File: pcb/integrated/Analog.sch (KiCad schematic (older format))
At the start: 47 parts, among them J5001 Conn_Coaxial, U5001 74LVC1G3157GW, U5002 TLV3501AIDBVR, U5003 74LVC1G3157GW, U5004 MCP6561-OT

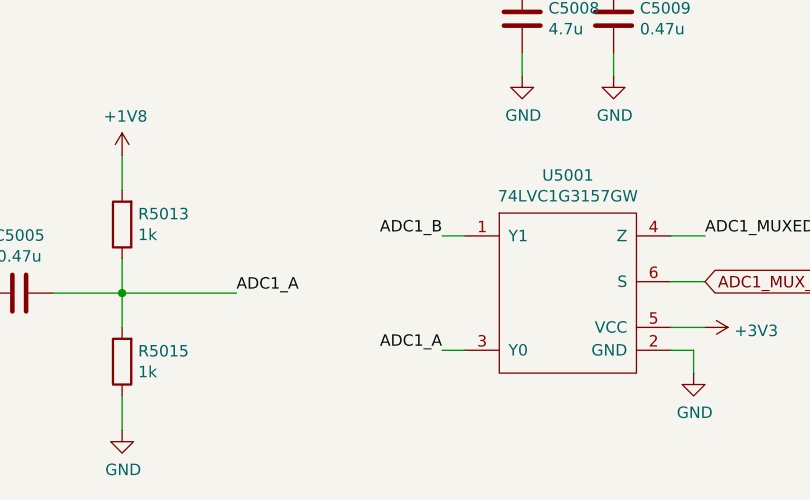
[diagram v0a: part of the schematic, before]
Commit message: schematic fixes and component placement
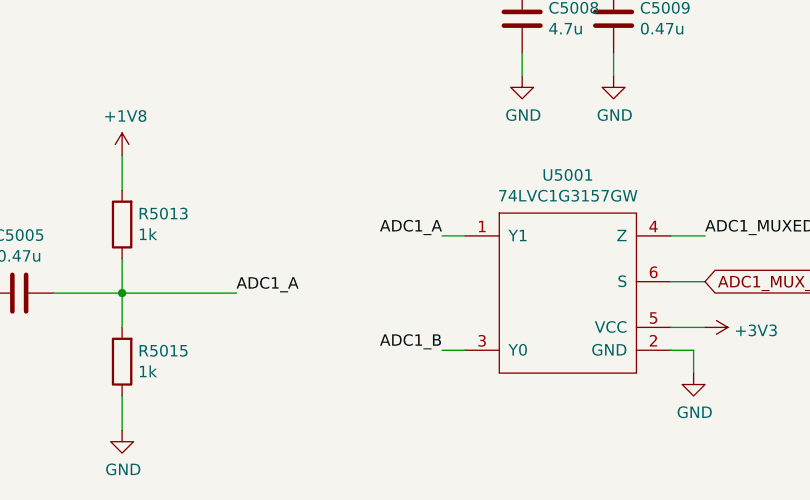
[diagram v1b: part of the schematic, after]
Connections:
- net ADC1_A: now also U5001.1 (Y1); no longer U5001.3 (Y0)
- net ADC1_B: now also U5001.3 (Y0); no longer U5001.1 (Y1)
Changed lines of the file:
@@
 Wire Wire Line
 	5150 7150 5050 7150
-Text Label 5050 7150 2    50   ~ 0
+Text Label 5050 6650 2    50   ~ 0
 ADC1_A
 $Comp
@@
 Text Label 2100 2350 0    50   ~ 0
 ADC1_B
-Text Label 5050 6650 2    50   ~ 0
+Text Label 5050 7150 2    50   ~ 0
 ADC1_B
 Wire Wire Line

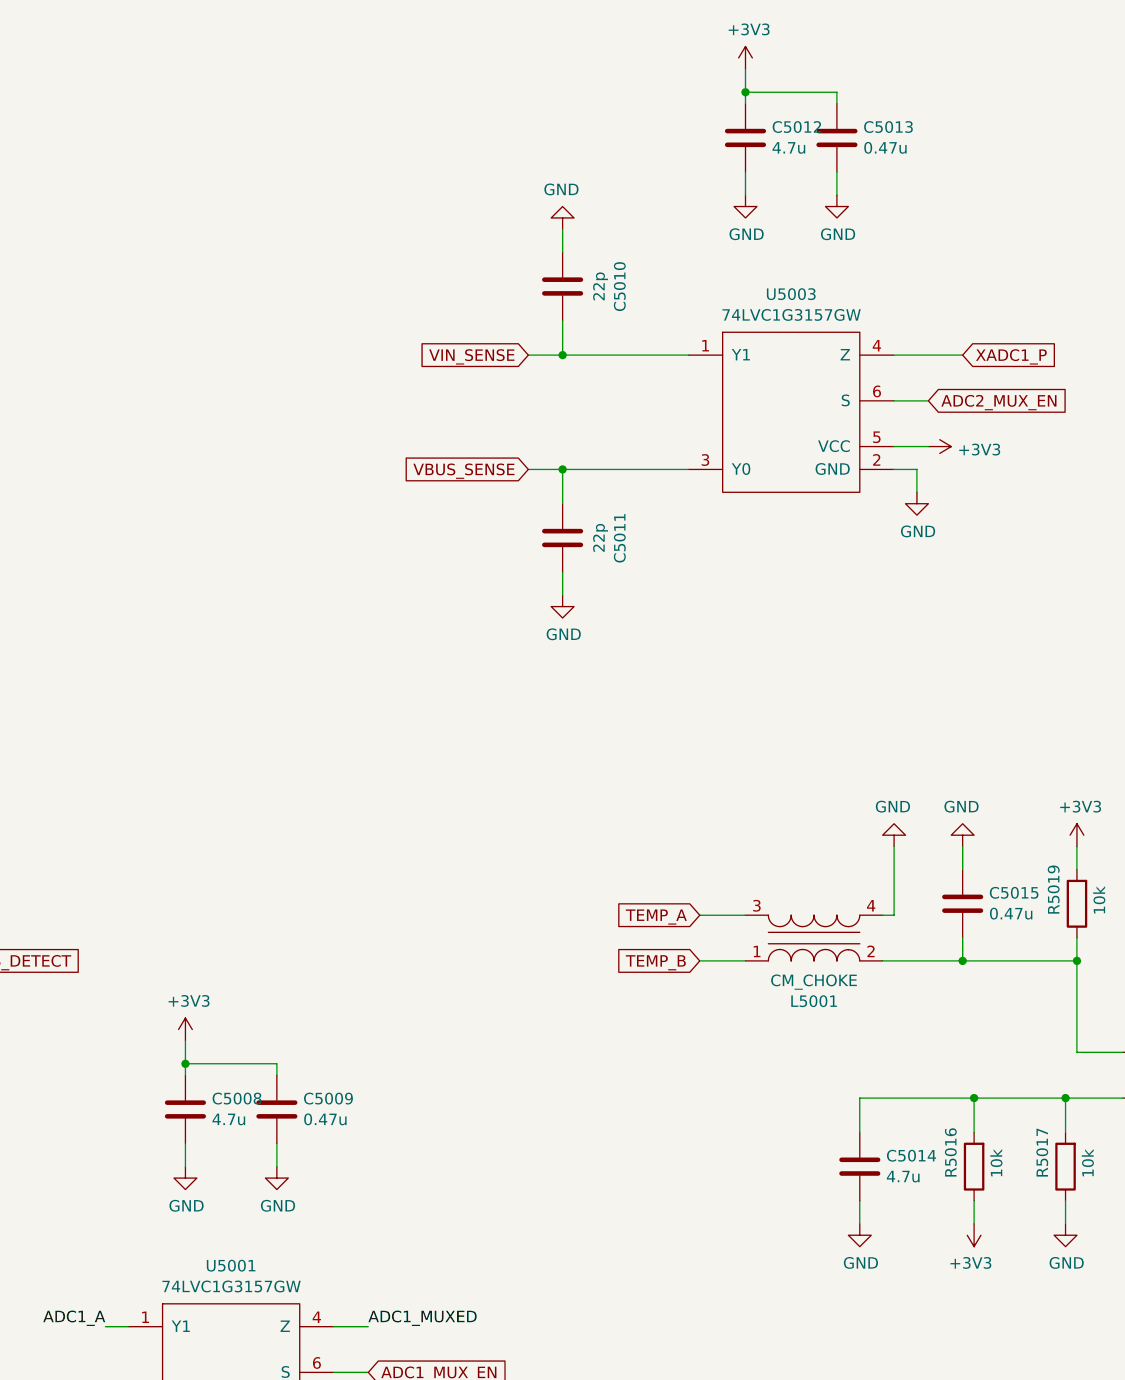
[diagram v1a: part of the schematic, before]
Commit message: routing, all componens placed on PCB
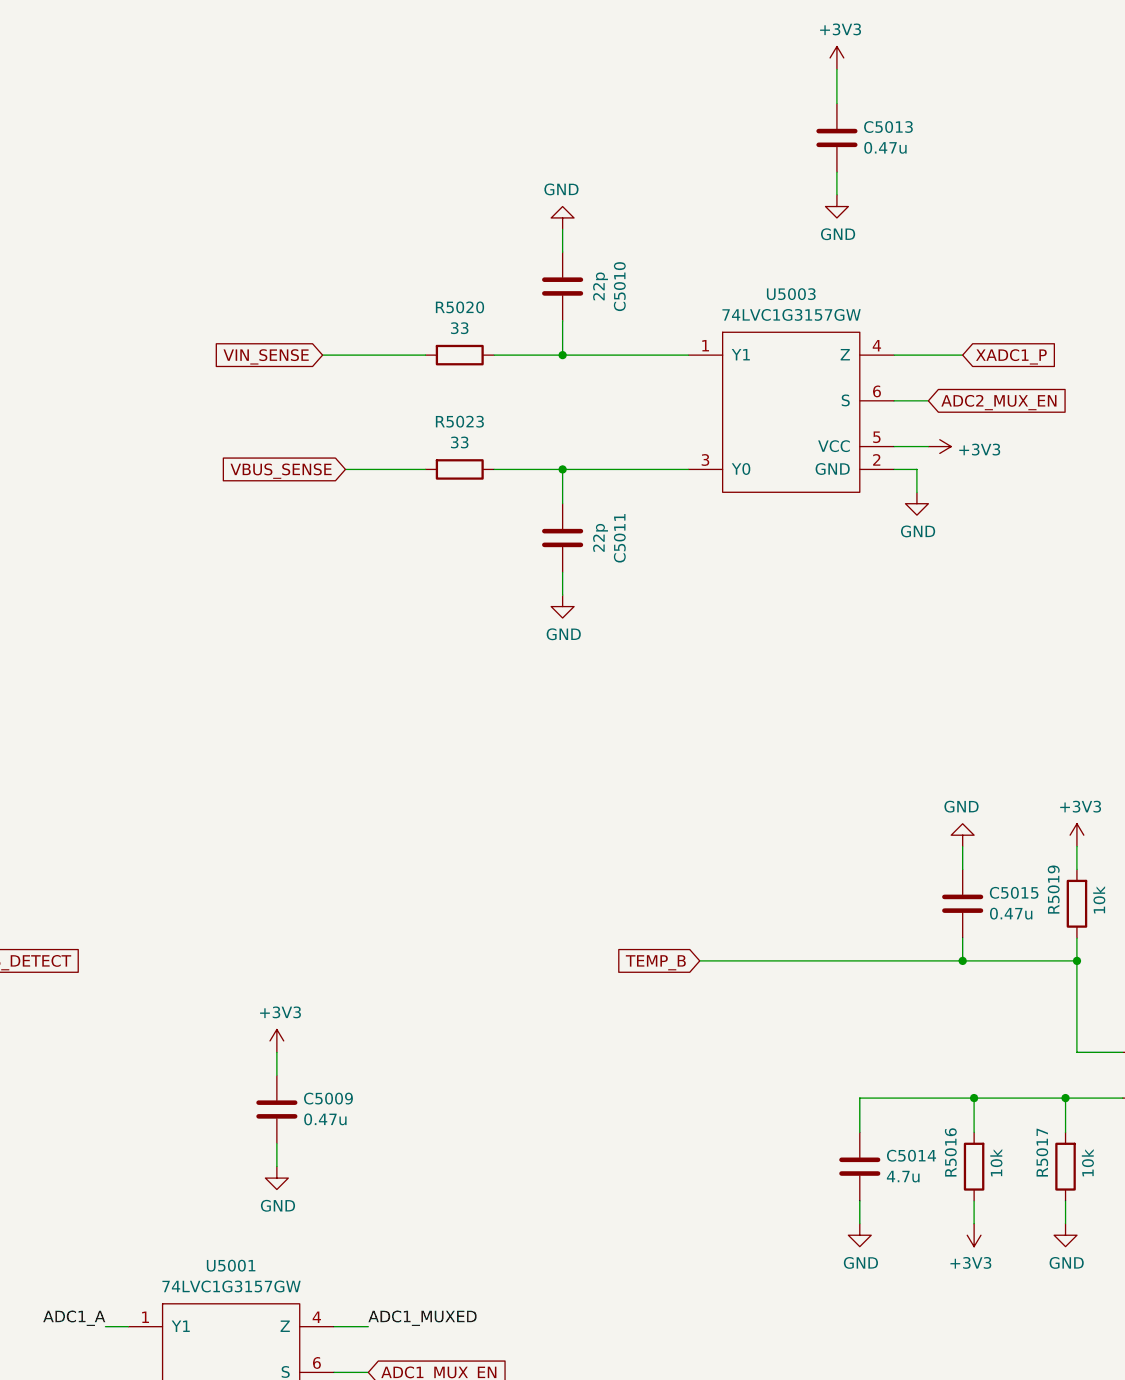
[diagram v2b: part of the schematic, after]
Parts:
- removed C5008, C5012: 4.7u, Capacitor_SMD:C_0402_1005Metric, symbol Device:C
- removed L5001: CM_CHOKE, wbraun_smd:SRF2012, symbol wbraun_ic_lib:CM_CHOKE
- added R5020, R5023: 33, Resistor_SMD:R_0402_1005Metric, symbol Device:R
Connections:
- net TEMP_B: now also C5015.1, R5019.1, U5004.3 (+)
- net VBUS_SENSE: now also R5023.2; no longer C5011.2, U5003.3 (Y0)
- net VIN_SENSE: now also R5020.2; no longer C5010.1, U5003.1 (Y1)
- new net: C5010.1, R5020.1, U5003.1 (Y1)
- new net: C5011.2, R5023.1, U5003.3 (Y0)
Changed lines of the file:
@@
 ADC1_MUXED
-$Comp
-L Device:C C5008
-U 1 1 5D844457
-P 5400 5700
-F 0 "C5008" H 5285 5654 50  0000 R CNN
-F 1 "4.7u" H 5285 5745 50  0000 R CNN
-F 2 "Capacitor_SMD:C_0402_1005Metric" H 5438 5550 50  0001 C CNN
-F 3 "~" H 5400 5700 50  0001 C CNN
-	1    5400 5700
-	-1   0    0    1
-$EndComp
 $Comp
 L Device:C C5009
@@
 $EndComp
 Wire Wire Line
-	5400 5500 5400 5550
-Wire Wire Line
-	5400 5500 5800 5500
-Wire Wire Line
-	5800 5500 5800 5550
-Wire Wire Line
-	5400 5850 5400 5950
-Wire Wire Line
 	5800 5850 5800 5950
 $Comp
@@
 	1    0    0    -1
 $EndComp
-$Comp
-L power:GND #PWR0129
-U 1 1 5D84446E
-P 5400 5950
-F 0 "#PWR0129" H 5400 5700 50  0001 C CNN
-F 1 "GND" H 5405 5777 50  0000 C CNN
-F 2 "" H 5400 5950 50  0001 C CNN
-F 3 "" H 5400 5950 50  0001 C CNN
-	1    5400 5950
-	1    0    0    -1
-$EndComp
-Wire Wire Line
-	5400 5500 5400 5400
-Connection ~ 5400 5500
+Wire Wire Line
+	5800 5550 5800 5450
 $Comp
 L power:+3V3 #PWR0130
 U 1 1 5D844476
-P 5400 5400
-F 0 "#PWR0130" H 5400 5250 50  0001 C CNN
-F 1 "+3V3" H 5415 5573 50  0000 C CNN
-F 2 "" H 5400 5400 50  0001 C CNN
-F 3 "" H 5400 5400 50  0001 C CNN
-	1    5400 5400
+P 5800 5450
+F 0 "#PWR0130" H 5800 5300 50  0001 C CNN
+F 1 "+3V3" H 5815 5623 50  0000 C CNN
+F 2 "" H 5800 5450 50  0001 C CNN
+F 3 "" H 5800 5450 50  0001 C CNN
+	1    5800 5450
 	1    0    0    -1
 $EndComp
@@
 	8600 2900 8600 3000
 $Comp
-L Device:C C5012
-U 1 1 5D875DF2
-P 7850 1450
-F 0 "C5012" H 7735 1404 50  0000 R CNN
-F 1 "4.7u" H 7735 1495 50  0000 R CNN
-F 2 "Capacitor_SMD:C_0402_1005Metric" H 7888 1300 50  0001 C CNN
-F 3 "~" H 7850 1450 50  0001 C CNN
-	1    7850 1450
-	-1   0    0    1
-$EndComp
-$Comp
 L Device:C C5013
 U 1 1 5D875DF8
@@
 $EndComp
 Wire Wire Line
-	7850 1250 7850 1300
-Wire Wire Line
-	7850 1250 8250 1250
-Wire Wire Line
-	8250 1250 8250 1300
-Wire Wire Line
-	7850 1600 7850 1700
-Wire Wire Line
 	8250 1600 8250 1700
 $Comp
@@
 $EndComp
 $Comp
-L power:GND #PWR0136
-U 1 1 5D875E09
-P 7850 1700
-F 0 "#PWR0136" H 7850 1450 50  0001 C CNN
-F 1 "GND" H 7855 1527 50  0000 C CNN
-F 2 "" H 7850 1700 50  0001 C CNN
-F 3 "" H 7850 1700 50  0001 C CNN
-	1    7850 1700
-	1    0    0    -1
-$EndComp
-Wire Wire Line
-	7850 1250 7850 1150
-Connection ~ 7850 1250
-$Comp
 L power:+3V3 #PWR0137
 U 1 1 5D875E11
-P 7850 1150
-F 0 "#PWR0137" H 7850 1000 50  0001 C CNN
-F 1 "+3V3" H 7865 1323 50  0000 C CNN
-F 2 "" H 7850 1150 50  0001 C CNN
-F 3 "" H 7850 1150 50  0001 C CNN
-	1    7850 1150
+P 8250 1150
+F 0 "#PWR0137" H 8250 1000 50  0001 C CNN
+F 1 "+3V3" H 8265 1323 50  0000 C CNN
+F 2 "" H 8250 1150 50  0001 C CNN
+F 3 "" H 8250 1150 50  0001 C CNN
+	1    8250 1150
 	1    0    0    -1
 $EndComp
@@
 $EndComp
 Wire Wire Line
-	7850 4850 7650 4850
-Wire Wire Line
-	7850 5050 7650 5050
-$Comp
-L wbraun_ic_lib:CM_CHOKE L?
-U 1 1 5D8C0AB3
-P 8150 4950
-AR Path="/5D68A538/5D8C0AB3" Ref="L?"  Part="1"
-AR Path="/5D68A538/5D62FC9C/5D8C0AB3" Ref="L?"  Part="1"
-AR Path="/5D68A538/5D640666/5D8C0AB3" Ref="L?"  Part="1"
-AR Path="/5D68A538/5D640674/5D8C0AB3" Ref="L?"  Part="1"
-AR Path="/5D68A538/5D640682/5D8C0AB3" Ref="L?"  Part="1"
-AR Path="/5D33C768/5D33CBF6/5D8C0AB3" Ref="L5001"  Part="1"
-F 0 "L5001" H 8150 5228 50  0000 C CNN
-F 1 "CM_CHOKE" H 8150 5137 50  0000 C CNN
-F 2 "wbraun_smd:SRF2012" V 8150 4950 50  0001 C CNN
-F 3 "" V 8150 4950 50  0000 C CNN
-	1    8150 4950
-	1    0    0    1
-$EndComp
-Wire Wire Line
 	9300 4550 9300 4650
 Wire Wire Line
@@
 Wire Wire Line
 	9300 5050 9300 4950
-$Comp
-L power:GND #PWR0148
-U 1 1 5D8F6FA4
-P 8500 4550
-F 0 "#PWR0148" H 8500 4300 50  0001 C CNN
-F 1 "GND" H 8505 4377 50  0000 C CNN
-F 2 "" H 8500 4550 50  0001 C CNN
-F 3 "" H 8500 4550 50  0001 C CNN
-	1    8500 4550
-	-1   0    0    1
-$EndComp
-Wire Wire Line
-	8450 4850 8500 4850
-Wire Wire Line
-	8500 4850 8500 4550
-Wire Wire Line
-	8450 5050 8800 5050
 Connection ~ 8800 5050
 Wire Wire Line
@@
 	9300 5450 9500 5450
 Connection ~ 9300 5050
-Text GLabel 7650 4850 0    50   Input ~ 0
-TEMP_A
 Text GLabel 7650 5050 0    50   Input ~ 0
 TEMP_B
@@
 Wire Wire Line
 	8500 2400 8800 2400
-Wire Wire Line
-	7050 2400 6900 2400
-Text GLabel 6900 2400 0    50   Input ~ 0
+Text GLabel 6000 2400 0    50   Input ~ 0
 VIN_SENSE
 $Comp
@@
 Wire Wire Line
 	7050 2900 7600 2900
-Wire Wire Line
-	7050 2900 6900 2900
 Connection ~ 7050 2900
-Text GLabel 6900 2900 0    50   Input ~ 0
+Text GLabel 6100 2900 0    50   Input ~ 0
 VBUS_SENSE
 $Comp
@@
 Wire Wire Line
 	7050 3350 7050 3450
+$Comp
+L Device:R R5020
+U 1 1 5DDA799E
+P 6600 2400
+F 0 "R5020" V 6393 2400 50  0000 C CNN
+F 1 "33" V 6484 2400 50  0000 C CNN
+F 2 "Resistor_SMD:R_0402_1005Metric" V 6530 2400 50  0001 C CNN
+F 3 "~" H 6600 2400 50  0001 C CNN
+	1    6600 2400
+	0    1    1    0
+$EndComp
+$Comp
+L Device:R R5023
+U 1 1 5DDA7D9F
+P 6600 2900
+F 0 "R5023" V 6393 2900 50  0000 C CNN
+F 1 "33" V 6484 2900 50  0000 C CNN
+F 2 "Resistor_SMD:R_0402_1005Metric" V 6530 2900 50  0001 C CNN
+F 3 "~" H 6600 2900 50  0001 C CNN
+	1    6600 2900
+	0    1    1    0
+$EndComp
+Wire Wire Line
+	6000 2400 6450 2400
+Wire Wire Line
+	6100 2900 6450 2900
+Wire Wire Line
+	6750 2900 7050 2900
+Wire Wire Line
+	6750 2400 7050 2400
+Wire Wire Line
+	7650 5050 8800 5050
+Wire Wire Line
+	8250 1150 8250 1300
 $EndSCHEMATC

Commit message: routing progress
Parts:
- removed C5016: 4.7u, Capacitor_SMD:C_0402_1005Metric, symbol Device:C
- C5014: value 4.7u -> 0.47u
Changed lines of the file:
@@
 P 8350 5950
 F 0 "C5014" H 8235 5904 50  0000 R CNN
-F 1 "4.7u" H 8235 5995 50  0000 R CNN
+F 1 "0.47u" H 8235 5995 50  0000 R CNN
 F 2 "Capacitor_SMD:C_0402_1005Metric" H 8388 5800 50  0001 C CNN
 F 3 "~" H 8350 5950 50  0001 C CNN
@@
 	9700 5850 9700 5950
 $Comp
-L Device:C C5016
-U 1 1 5D8B2312
-P 10100 4850
-F 0 "C5016" H 9985 4804 50  0000 R CNN
-F 1 "4.7u" H 9985 4895 50  0000 R CNN
-F 2 "Capacitor_SMD:C_0402_1005Metric" H 10138 4700 50  0001 C CNN
-F 3 "~" H 10100 4850 50  0001 C CNN
-	1    10100 4850
-	-1   0    0    1
-$EndComp
-$Comp
 L Device:C C5017
 U 1 1 5D8B2318
@@
 $EndComp
 Wire Wire Line
-	10100 4650 10100 4700
-Wire Wire Line
-	10100 4650 10500 4650
-Wire Wire Line
-	10500 4650 10500 4700
-Wire Wire Line
-	10100 5000 10100 5100
-Wire Wire Line
 	10500 5000 10500 5100
 $Comp
@@
 $EndComp
 $Comp
-L power:GND #PWR0144
-U 1 1 5D8B2329
-P 10100 5100
-F 0 "#PWR0144" H 10100 4850 50  0001 C CNN
-F 1 "GND" H 10105 4927 50  0000 C CNN
-F 2 "" H 10100 5100 50  0001 C CNN
-F 3 "" H 10100 5100 50  0001 C CNN
-	1    10100 5100
-	1    0    0    -1
-$EndComp
-Wire Wire Line
-	10100 4650 10100 4550
-Connection ~ 10100 4650
-$Comp
 L power:+3V3 #PWR0145
 U 1 1 5D8B2331
-P 10100 4550
-F 0 "#PWR0145" H 10100 4400 50  0001 C CNN
-F 1 "+3V3" H 10115 4723 50  0000 C CNN
-F 2 "" H 10100 4550 50  0001 C CNN
-F 3 "" H 10100 4550 50  0001 C CNN
-	1    10100 4550
+P 10500 4550
+F 0 "#PWR0145" H 10500 4400 50  0001 C CNN
+F 1 "+3V3" H 10515 4723 50  0000 C CNN
+F 2 "" H 10500 4550 50  0001 C CNN
+F 3 "" H 10500 4550 50  0001 C CNN
+	1    10500 4550
 	1    0    0    -1
 $EndComp
@@
 Wire Wire Line
 	8250 1150 8250 1300
+Wire Wire Line
+	10500 4550 10500 4700
 $EndSCHEMATC

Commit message: PCB routing finihsed, ready for design review
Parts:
- added R5024, R5025, R5026, R5027: 33, Resistor_SMD:R_0402_1005Metric, symbol Device:R
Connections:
- net GND: now also R5024.1, R5026.2
- net TEMP_B: now also R5025.2; no longer C5015.1, R5019.1, U5004.3 (+)
- net VBUS_SENSE: now also R5020.2; no longer R5023.2
- net VIN_SENSE: now also R5023.2; no longer R5020.2
- net XADC1_P: now also R5027.1; no longer U5003.4 (Z)
- new net: R5027.2, U5003.4 (Z)
- new net: C5015.1, R5019.1, R5025.1, U5004.3 (+)
- new net TEMP_A: R5024.2
- new net XADC1_N: R5026.1
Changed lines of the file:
@@
 Wire Wire Line
 	9300 5050 9300 4950
-Connection ~ 8800 5050
 Wire Wire Line
 	9300 5050 9300 5450
@@
 	1    0    0    -1
 $EndComp
-Text GLabel 8800 2400 2    50   Input ~ 0
+Text GLabel 9150 2400 2    50   Input ~ 0
 XADC1_P
 Wire Wire Line
 	8500 2400 8800 2400
-Text GLabel 6000 2400 0    50   Input ~ 0
+Text GLabel 6100 2900 0    50   Input ~ 0
 VIN_SENSE
 $Comp
@@
 	7050 2900 7600 2900
 Connection ~ 7050 2900
-Text GLabel 6100 2900 0    50   Input ~ 0
+Text GLabel 6000 2400 0    50   Input ~ 0
 VBUS_SENSE
 $Comp
@@
 	6750 2400 7050 2400
 Wire Wire Line
-	7650 5050 8800 5050
-Wire Wire Line
 	8250 1150 8250 1300
 Wire Wire Line
 	10500 4550 10500 4700
+$Comp
+L Device:R R5024
+U 1 1 5DD2E6C4
+P 8050 4700
+F 0 "R5024" V 7843 4700 50  0000 C CNN
+F 1 "33" V 7934 4700 50  0000 C CNN
+F 2 "Resistor_SMD:R_0402_1005Metric" V 7980 4700 50  0001 C CNN
+F 3 "~" H 8050 4700 50  0001 C CNN
+	1    8050 4700
+	0    1    1    0
+$EndComp
+Text GLabel 7650 4700 0    50   Input ~ 0
+TEMP_A
+$Comp
+L power:GND #PWR0136
+U 1 1 5DD2F9F0
+P 8350 4600
+F 0 "#PWR0136" H 8350 4350 50  0001 C CNN
+F 1 "GND" H 8355 4427 50  0000 C CNN
+F 2 "" H 8350 4600 50  0001 C CNN
+F 3 "" H 8350 4600 50  0001 C CNN
+	1    8350 4600
+	-1   0    0    1
+$EndComp
+Wire Wire Line
+	7650 4700 7900 4700
+Wire Wire Line
+	8200 4700 8350 4700
+Wire Wire Line
+	8350 4700 8350 4600
+$Comp
+L Device:R R5025
+U 1 1 5DD397B5
+P 8050 5050
+F 0 "R5025" V 7843 5050 50  0000 C CNN
+F 1 "33" V 7934 5050 50  0000 C CNN
+F 2 "Resistor_SMD:R_0402_1005Metric" V 7980 5050 50  0001 C CNN
+F 3 "~" H 8050 5050 50  0001 C CNN
+	1    8050 5050
+	0    1    1    0
+$EndComp
+Wire Wire Line
+	7650 5050 7900 5050
+Wire Wire Line
+	8200 5050 8800 5050
+Connection ~ 8800 5050
+$Comp
+L Device:R R5027
+U 1 1 5DD500FB
+P 8950 2400
+F 0 "R5027" V 8743 2400 50  0000 C CNN
+F 1 "33" V 8834 2400 50  0000 C CNN
+F 2 "Resistor_SMD:R_0402_1005Metric" V 8880 2400 50  0001 C CNN
+F 3 "~" H 8950 2400 50  0001 C CNN
+	1    8950 2400
+	0    1    1    0
+$EndComp
+$Comp
+L Device:R R5026
+U 1 1 5DD507F4
+P 8950 1950
+F 0 "R5026" V 8743 1950 50  0000 C CNN
+F 1 "33" V 8834 1950 50  0000 C CNN
+F 2 "Resistor_SMD:R_0402_1005Metric" V 8880 1950 50  0001 C CNN
+F 3 "~" H 8950 1950 50  0001 C CNN
+	1    8950 1950
+	0    1    1    0
+$EndComp
+Text GLabel 9200 1950 2    50   Input ~ 0
+XADC1_N
+Wire Wire Line
+	9100 1950 9200 1950
+Wire Wire Line
+	9100 2400 9150 2400
+$Comp
+L power:GND #PWR0144
+U 1 1 5DD5AEA8
+P 8750 1950
+F 0 "#PWR0144" H 8750 1700 50  0001 C CNN
+F 1 "GND" H 8755 1777 50  0000 C CNN
+F 2 "" H 8750 1950 50  0001 C CNN
+F 3 "" H 8750 1950 50  0001 C CNN
+	1    8750 1950
+	0    1    1    0
+$EndComp
+Wire Wire Line
+	8800 1950 8750 1950
 $EndSCHEMATC
